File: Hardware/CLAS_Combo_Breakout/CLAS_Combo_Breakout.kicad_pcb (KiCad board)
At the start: 4 copper layers, 60 x 60 mm, 88 parts, among them J1 USB_C_Receptacle_USB2.0, J2 ZED, J3 NEO, J4 USB_C_Receptacle_USB2.0, J5 Conn_SMA, U1 USBLC6-2P6, U10 NT1191GEAE3S, U2 ZED-F9P, U3 NEO-D9C-00B, U4 USBLC6-2P6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

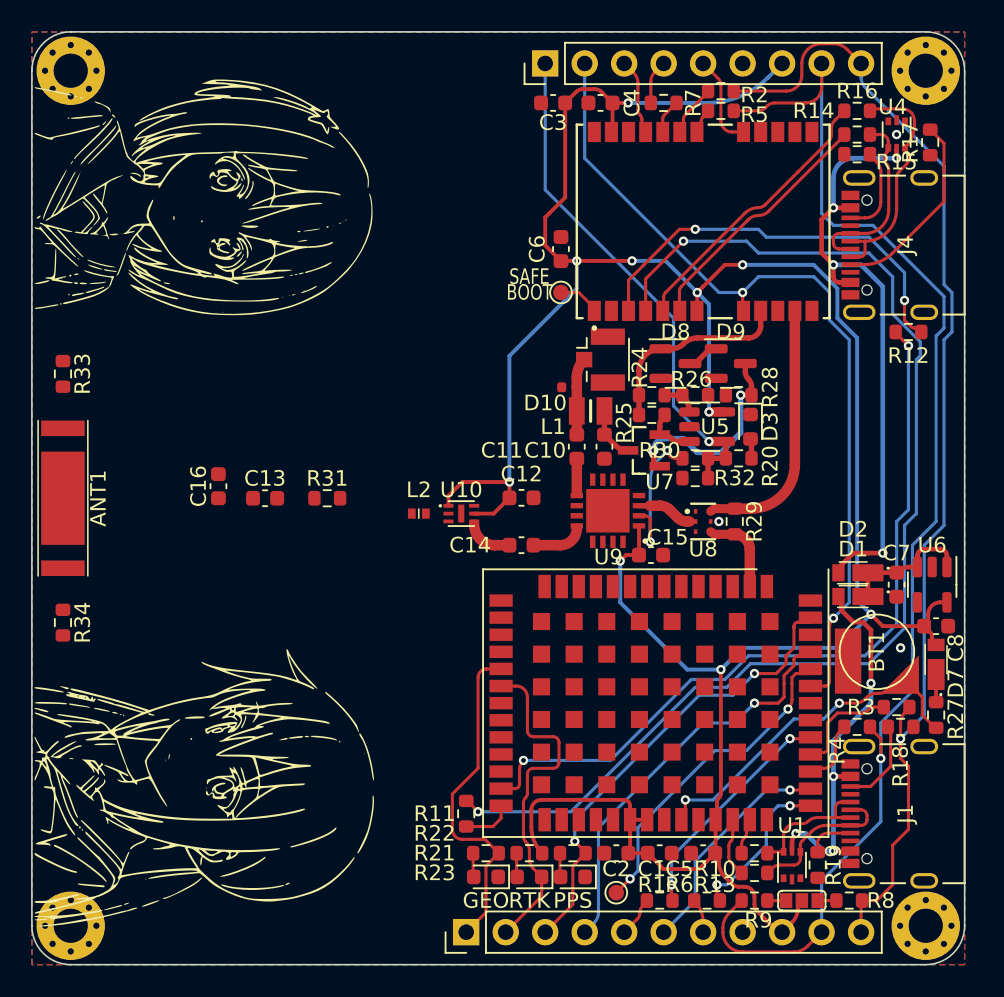
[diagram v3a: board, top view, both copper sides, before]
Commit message: 伝送線路にビアを配置part1
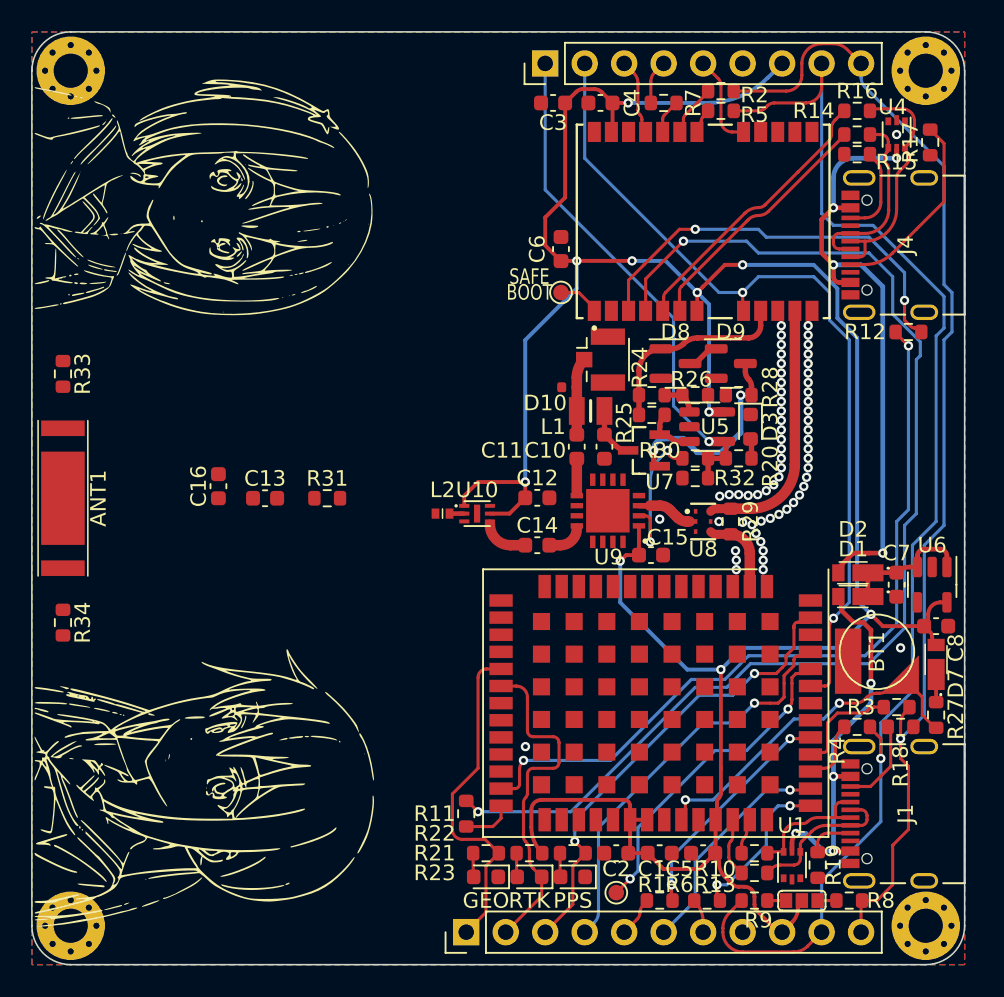
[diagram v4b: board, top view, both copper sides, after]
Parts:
- moved L2 1.52 mm to (126.4, 121.0)
- moved U10 1.02 mm to (128.6, 121.0)
- moved C12 1.02 mm to (132.5, 120.0)
- moved C14 1.02 mm to (132.5, 123.0)
- moved R29 0.25 mm to (145.0, 121.5)
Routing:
- net Net-(C14-Pad1): track 3.35 -> 2.33 mm
- net Net-(L2-Pad2): track 0.00 -> 0.95 mm
- net GND: vias 3 -> 63

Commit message: アンテナ設計中
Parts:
- removed the G*** at (111.2, 138.8)
- removed the G*** at (118.8, 95.6)
- removed the G*** at (111.2, 100.7)
- added G***: LOGO, LOGO_CLAS_Receiver:CLAS_Receiver, F.Cu at (117.8, 94.6)
- moved R33 1.62 mm to (100.7, 112.9)
- moved R34 1.62 mm to (100.7, 127.1)
- moved C13 1.00 mm to (114.0, 120.0)
- moved C16 1.00 mm to (111.0, 119.2)
- moved R31 1.00 mm to (118.0, 120.0)
- moved ANT1 0.40 mm to (101.6, 120.0)
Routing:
- net GND: vias 63 -> 174
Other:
- board text added: "3V3"
- board text added: "EXTANT_DETECT"
- board text added: "EXTINT_NEO"
- board text added: "EXTINT_ZED"
- board text added: "GND"
- board text added: "RESET"
- board text added: "RXD1_NEO"
- board text added: "RXD1_ZED"
- board text added: "SCL"
- board text added: "SDA"
- board text added: "TXD1_NEO"
- board text added: "TXD1_ZED"
- board text added: "TX_RDY"

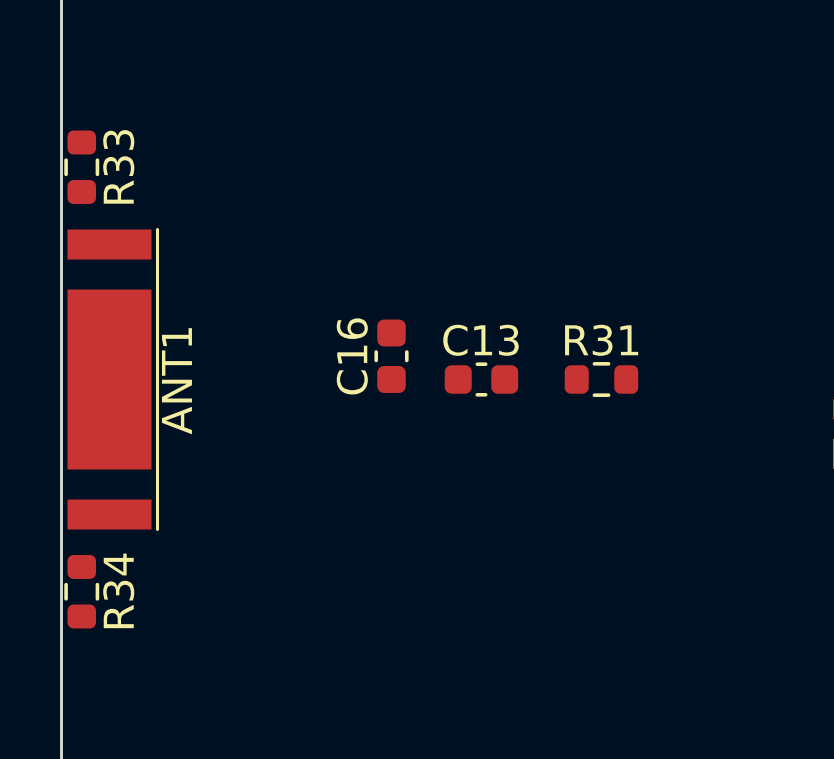
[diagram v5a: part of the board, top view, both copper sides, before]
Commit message: アンテナ周りを配線
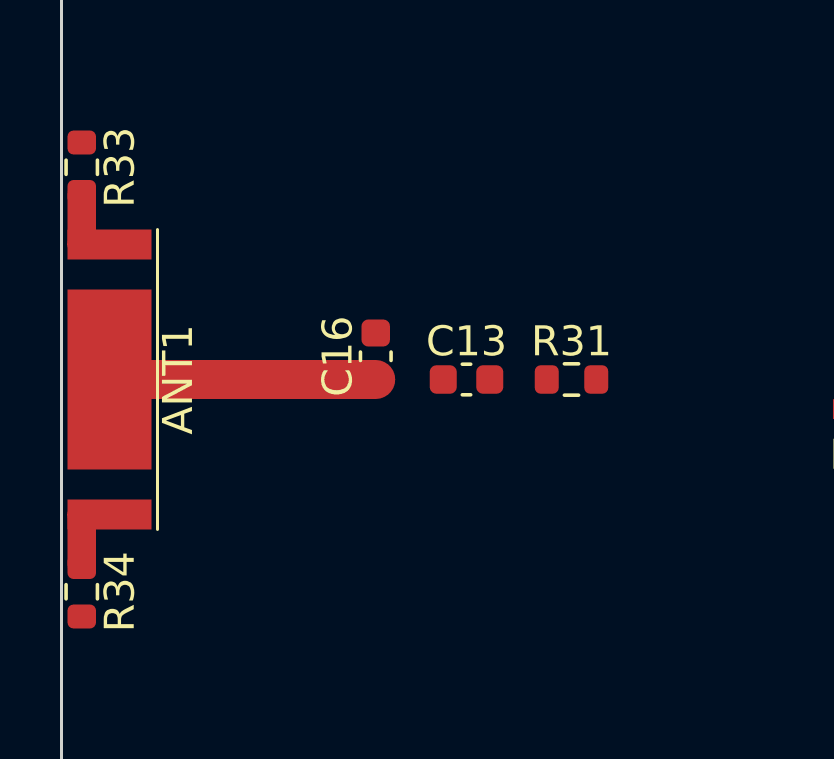
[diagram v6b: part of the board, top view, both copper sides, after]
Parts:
- moved R31 1.00 mm to (117.0, 120.0)
- moved C16 0.53 mm to (110.5, 119.2)
- moved C13 0.50 mm to (113.5, 120.0)
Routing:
- net Net-(ANT1-Pad1): track 0.00 -> 8.88 mm
- net Net-(ANT1-Pad3): track 0.00 -> 2.60 mm
- net Net-(ANT1-Pad2): track 0.00 -> 2.60 mm
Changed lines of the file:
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@@
   )
   (footprint "Resistor_SMD:R_0603_1608Metric" (layer "F.Cu")
-    (at 118 120)
+    (at 117 120)
     (descr "Resistor SMD 0603 (1608 Metric), square (rectangular) end terminal, IPC_7351 nominal, (Body size source: IPC-SM-782 page 72, https://www.pcb-3d.com/wordpress/wp-content/uploads/ipc-sm-782a_amendment_1_and_2.pdf), generated with kicad-footprint-generator")
     (tags "resistor")
@@
   )
   (footprint "Capacitor_SMD:C_0603_1608Metric" (layer "F.Cu")
-    (at 114 120)
+    (at 113.5 120)
     (descr "Capacitor SMD 0603 (1608 Metric), square (rectangular) end terminal, IPC_7351 nominal, (Body size source: IPC-SM-782 page 76, https://www.pcb-3d.com/wordpress/wp-content/uploads/ipc-sm-782a_amendment_1_and_2.pdf), generated with kicad-footprint-generator")
     (tags "capacitor")
@@
   )
   (footprint "Capacitor_SMD:C_0603_1608Metric" (layer "F.Cu")
-    (at 111 119.225 90)
+    (at 110.475 119.225 90)
     (descr "Capacitor SMD 0603 (1608 Metric), square (rectangular) end terminal, IPC_7351 nominal, (Body size source: IPC-SM-782 page 76, https://www.pcb-3d.com/wordpress/wp-content/uploads/ipc-sm-782a_amendment_1_and_2.pdf), generated with kicad-footprint-generator")
     (tags "capacitor")
@@
     (effects (font (size 1 0.75) (thickness 0.15)))
   )
+  (segment (start 101.6 120) (end 110.475 120) (width 1.3) (layer "F.Cu") (net 1))
+  (segment (start 101.6 115.5) (end 100.675 115.5) (width 0.95) (layer "F.Cu") (net 2))
+  (segment (start 100.675 115.5) (end 100.675 113.825) (width 0.95) (layer "F.Cu") (net 2))
+  (segment (start 101.6 124.5) (end 100.675 124.5) (width 0.95) (layer "F.Cu") (net 3))
+  (segment (start 100.675 124.5) (end 100.675 126.175) (width 0.95) (layer "F.Cu") (net 3))
   (segment (start 157.277 133.942) (end 157.277 132.789) (width 0.2) (layer "F.Cu") (net 4))
   (segment (start 156.061957 131.9) (end 156.388 131.9) (width 0.2) (layer "F.Cu") (net 4))

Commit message: 伝送線路配線完了
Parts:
- added C9: DNF, Capacitor_SMD:C_0603_1608Metric, F.Cu at (115.5, 119.2)
- moved R31 1.00 mm to (118.0, 120.0)
- moved C13 0.50 mm to (113.0, 120.0)
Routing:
- net Net-(L2-Pad1): track 0.00 -> 7.39 mm
- net Net-(C13-Pad2): track 0.00 -> 3.40 mm
- net Net-(ANT1-Pad1): track 8.88 -> 10.6 mm
- net GND: vias 174 -> 281
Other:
- board text added: "DNF"

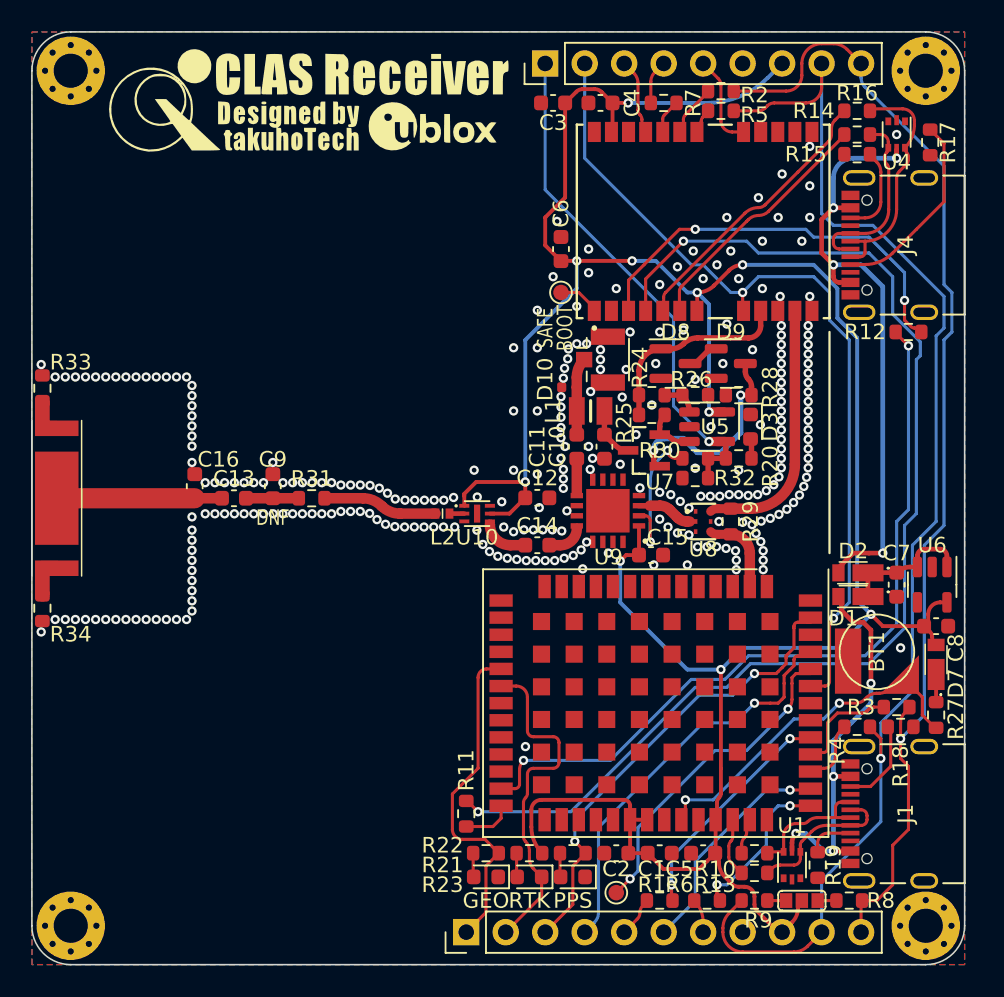
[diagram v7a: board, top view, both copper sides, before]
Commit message: 上半分にビアを配置
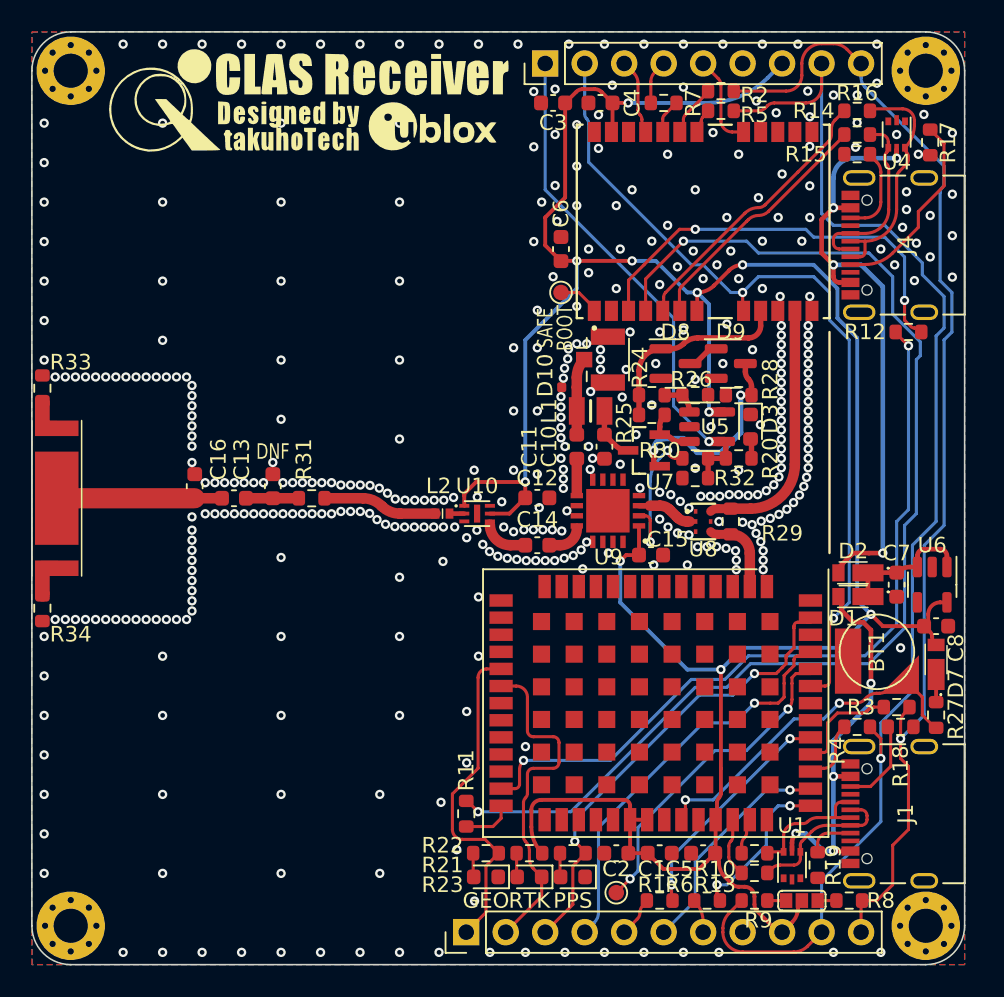
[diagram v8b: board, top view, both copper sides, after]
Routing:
- net Net-(R12-Pad2): track 26.8 -> 27.4 mm
- net GND: vias 281 -> 414
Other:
- board text added: "外周にビアを置くときは、基板中心を原点にする"
